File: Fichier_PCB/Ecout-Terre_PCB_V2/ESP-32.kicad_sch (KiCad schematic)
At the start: 43 parts, among them J10 Micro_SD_Card, J13 Conn_GPS, J5 Conn_Alim, J7 Conn_ESP, J8 Conn_ESP, U4 PCM1804, U7 74LVT04, Y1 7V-22.5792MAHV-T

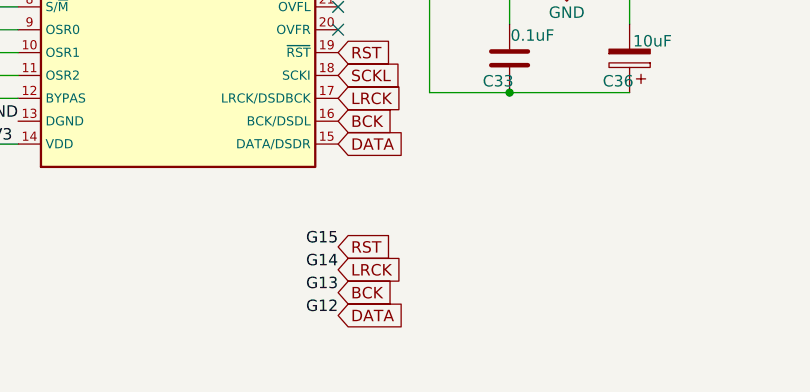
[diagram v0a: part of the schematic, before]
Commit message: Trace pcb
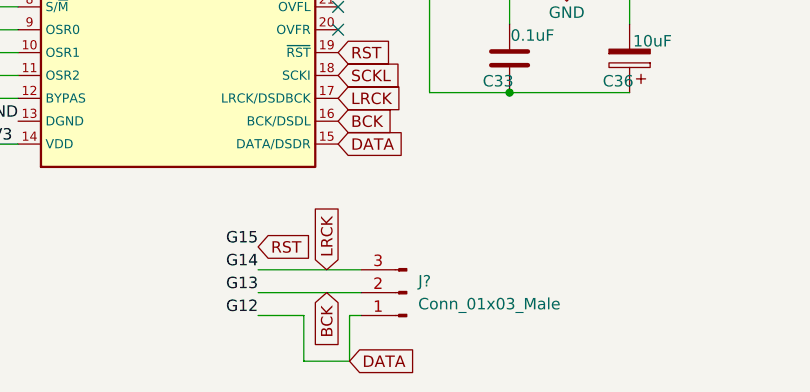
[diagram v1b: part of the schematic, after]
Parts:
- added J?: Conn_01x03_Male, Connector_PinHeader_2.54mm:PinHeader_1x03_P2.54mm_Vertical, symbol Connector:Conn_01x03_Male
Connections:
- net BCK: now also J?.2 (Pin_2)
- net DATA: now also J?.1 (Pin_1)
- net LRCK: now also J?.3 (Pin_3)
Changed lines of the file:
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@@
+    (stroke (width 0) (type default) (color 0 0 0 0))
+  )
+  (wire (pts (xy 97.79 172.72) (xy 102.87 172.72))
     (stroke (width 0) (type default) (color 0 0 0 0))
   )
@@
     (stroke (width 0) (type default) (color 0 0 0 0))
   )
+  (wire (pts (xy 102.87 172.72) (xy 102.87 167.64))
+    (stroke (width 0) (type default) (color 0 0 0 0))
+  )
   (wire (pts (xy 45.085 128.27) (xy 49.53 128.27))
     (stroke (width 0) (type default) (color 0 0 0 0))
@@
     (stroke (width 0) (type default) (color 0 0 0 0))
   )
+  (wire (pts (xy 102.87 167.64) (xy 104.14 167.64))
+    (stroke (width 0) (type default) (color 0 0 0 0))
+  )
   (wire (pts (xy 133.985 128.27) (xy 133.985 135.255))
     (stroke (width 0) (type default) (color 0 0 0 0))
@@
     (stroke (width 0) (type default) (color 0 0 0 0))
   )
+  (wire (pts (xy 92.71 167.64) (xy 97.79 167.64))
+    (stroke (width 0) (type default) (color 0 0 0 0))
+  )
   (wire (pts (xy 111.76 142.875) (xy 120.65 142.875))
     (stroke (width 0) (type default) (color 0 0 0 0))
@@
     (stroke (width 0) (type default) (color 0 0 0 0))
   )
+  (wire (pts (xy 92.71 165.1) (xy 104.14 165.1))
+    (stroke (width 0) (type default) (color 0 0 0 0))
+  )
   (wire (pts (xy 58.42 93.98) (xy 58.42 90.17))
     (stroke (width 0) (type default) (color 0 0 0 0))
@@
     (stroke (width 0) (type default) (color 0 0 0 0))
   )
+  (wire (pts (xy 97.79 167.64) (xy 97.79 172.72))
+    (stroke (width 0) (type default) (color 0 0 0 0))
+  )
   (wire (pts (xy 40.64 62.23) (xy 36.83 62.23))
     (stroke (width 0) (type default) (color 0 0 0 0))
@@
     (stroke (width 0) (type default) (color 0 0 0 0))
   )
+  (wire (pts (xy 92.71 162.56) (xy 104.14 162.56))
+    (stroke (width 0) (type default) (color 0 0 0 0))
+  )
   (wire (pts (xy 173.99 121.92) (xy 182.88 121.92))
     (stroke (width 0) (type default) (color 0 0 0 0))
@@
     (effects (font (size 1.27 1.27)) (justify right bottom))
   )
-  (label "G15" (at 101.6 160.02 180)
+  (label "G15" (at 92.71 160.02 180)
     (effects (font (size 1.27 1.27)) (justify right bottom))
   )
@@
     (effects (font (size 1.27 1.27)) (justify right bottom))
   )
-  (label "G12" (at 101.6 167.64 180)
+  (label "G12" (at 92.71 167.64 180)
     (effects (font (size 1.27 1.27)) (justify right bottom))
   )
@@
     (effects (font (size 1.27 1.27)) (justify left bottom))
   )
-  (label "G14" (at 101.6 162.56 180)
+  (label "G14" (at 92.71 162.56 180)
     (effects (font (size 1.27 1.27)) (justify right bottom))
   )
@@
     (effects (font (size 1.27 1.27)) (justify right bottom))
   )
-  (label "G13" (at 101.6 165.1 180)
+  (label "G13" (at 92.71 165.1 180)
     (effects (font (size 1.27 1.27)) (justify right bottom))
   )
@@
     (effects (font (size 1.27 1.27)) (justify right bottom))
   )
-  (global_label "DATA" (shape input) (at 101.6 167.64 0) (fields_autoplaced)
-    (effects (font (size 1.27 1.27)) (justify left))
-    (property "Intersheet References" "${INTERSHEET_REFS}" (id 0) (at 108.4279 167.5606 0)
+  (global_label "DATA" (shape input) (at 102.87 172.72 0) (fields_autoplaced)
+    (effects (font (size 1.27 1.27)) (justify left))
+    (property "Intersheet References" "${INTERSHEET_REFS}" (id 0) (at 109.6979 172.6406 0)
       (effects (font (size 1.27 1.27)) (justify left) hide)
     )
@@
     )
   )
-  (global_label "LRCK" (shape input) (at 101.6 162.56 0) (fields_autoplaced)
-    (effects (font (size 1.27 1.27)) (justify left))
-    (property "Intersheet References" "${INTERSHEET_REFS}" (id 0) (at 108.8512 162.4806 0)
+  (global_label "LRCK" (shape input) (at 100.33 162.56 90) (fields_autoplaced)
+    (effects (font (size 1.27 1.27)) (justify left))
+    (property "Intersheet References" "${INTERSHEET_REFS}" (id 0) (at 100.2506 155.3088 90)
       (effects (font (size 1.27 1.27)) (justify left) hide)
     )
@@
     )
   )
-  (global_label "BCK" (shape input) (at 101.6 165.1 0) (fields_autoplaced)
-    (effects (font (size 1.27 1.27)) (justify left))
-    (property "Intersheet References" "${INTERSHEET_REFS}" (id 0) (at 107.8231 165.0206 0)
-      (effects (font (size 1.27 1.27)) (justify left) hide)
-    )
-  )
-  (global_label "RST" (shape input) (at 101.6 160.02 0) (fields_autoplaced)
-    (effects (font (size 1.27 1.27)) (justify left))
-    (property "Intersheet References" "${INTERSHEET_REFS}" (id 0) (at 107.4602 159.9406 0)
+  (global_label "BCK" (shape input) (at 100.33 165.1 270) (fields_autoplaced)
+    (effects (font (size 1.27 1.27)) (justify right))
+    (property "Intersheet References" "${INTERSHEET_REFS}" (id 0) (at 100.4094 171.3231 90)
+      (effects (font (size 1.27 1.27)) (justify right) hide)
+    )
+  )
+  (global_label "RST" (shape input) (at 92.71 160.02 0) (fields_autoplaced)
+    (effects (font (size 1.27 1.27)) (justify left))
+    (property "Intersheet References" "${INTERSHEET_REFS}" (id 0) (at 98.5702 159.9406 0)
       (effects (font (size 1.27 1.27)) (justify left) hide)
     )
@@
     (pin "2")
   )
+  (symbol (lib_id "Connector:Conn_01x03_Male") (at 109.22 165.1 180) (unit 1)
+    (in_bom yes) (on_board yes) (fields_autoplaced)
+    (property "Reference" "J?" (id 0) (at 110.49 163.8299 0)
+      (effects (font (size 1.27 1.27)) (justify right))
+    )
+    (property "Value" "Conn_01x03_Male" (id 1) (at 110.49 166.3699 0)
+      (effects (font (size 1.27 1.27)) (justify right))
+    )
+    (property "Footprint" "Connector_PinHeader_2.54mm:PinHeader_1x03_P2.54mm_Vertical" (id 2) (at 109.22 165.1 0)
+      (effects (font (size 1.27 1.27)) hide)
+    )
+    (property "Datasheet" "~" (id 3) (at 109.22 165.1 0)
+      (effects (font (size 1.27 1.27)) hide)
+    )
+    (pin "1")
+    (pin "2")
+    (pin "3")
+  )
   (symbol (lib_id "Device:C_Polarized") (at 133.985 139.065 180) (unit 1)

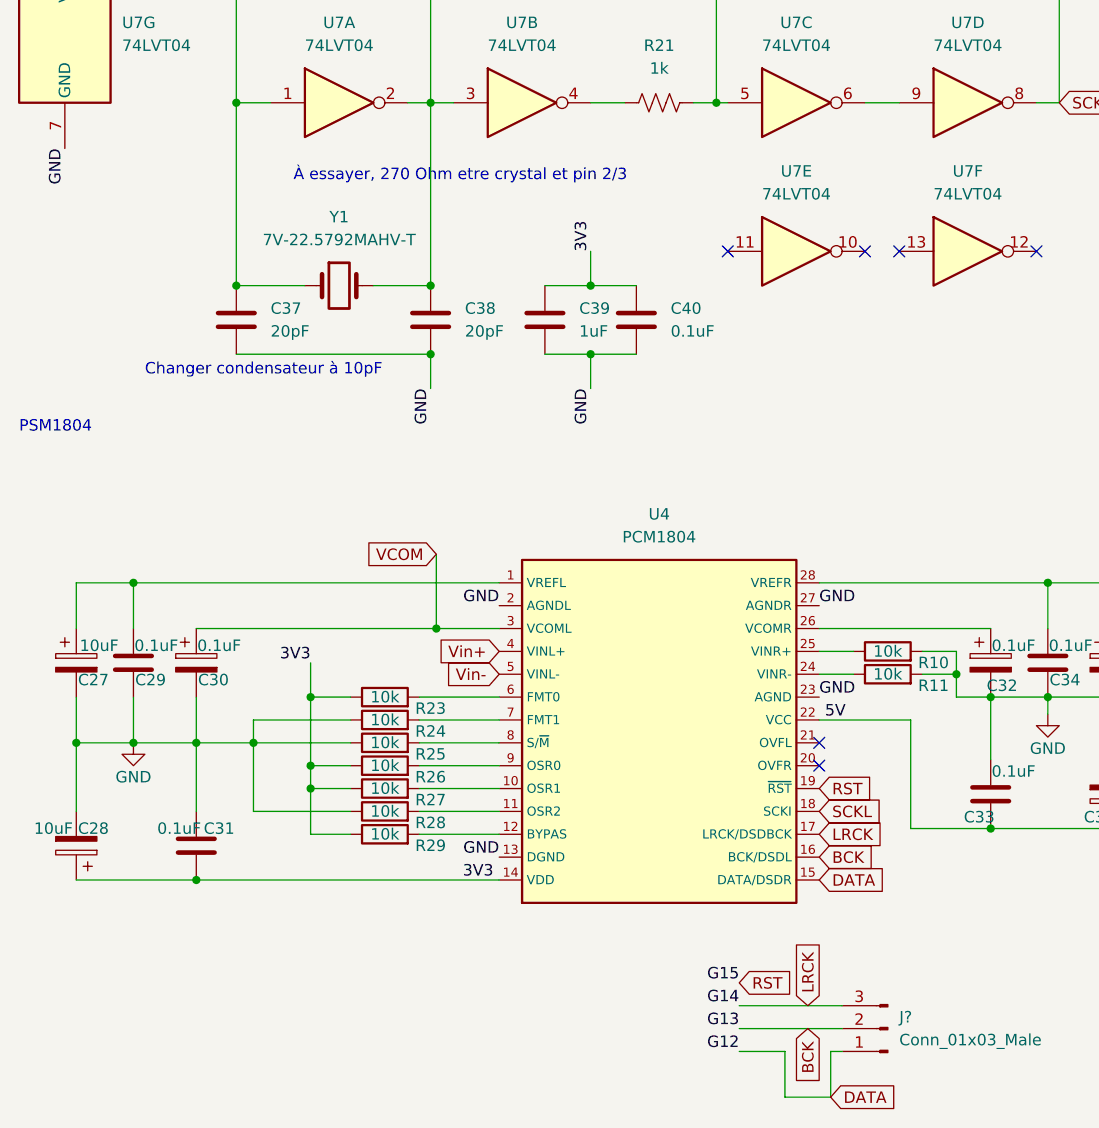
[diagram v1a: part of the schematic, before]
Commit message: Envoie de code et correction PCB
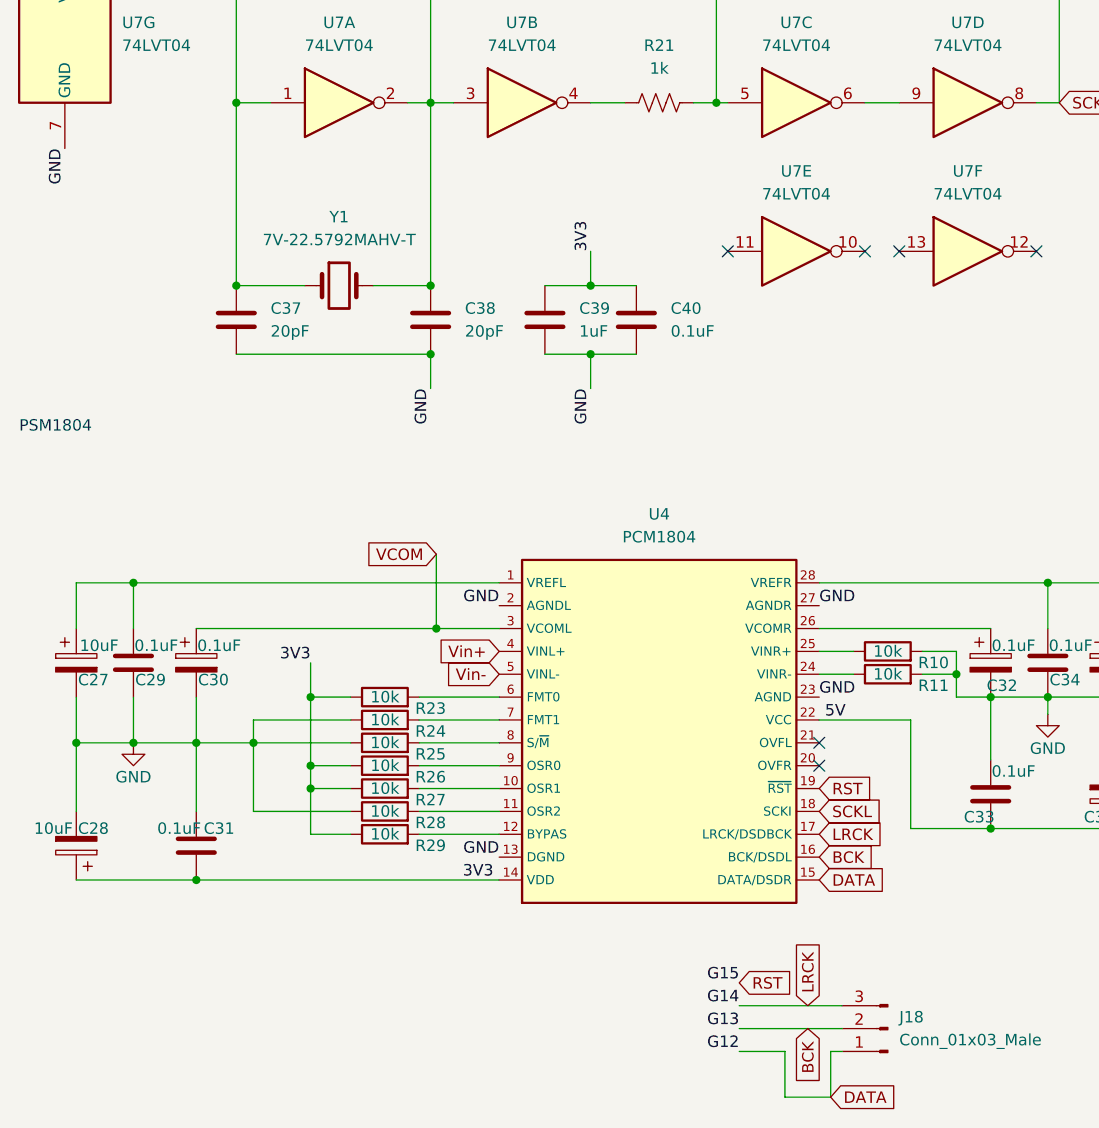
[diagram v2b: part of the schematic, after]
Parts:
- gave numbers to parts that had none: 1
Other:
- note removed: "Changer condensateur à 10pF"
- note removed: "À essayer, 270 Ohm etre crystal et pin 2/3"
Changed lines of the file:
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@@
-    (effects (font (size 1.27 1.27)) (justify left bottom))
-  )
-  (text "Changer condensateur à 10pF" (at 26.67 92.71 0)
     (effects (font (size 1.27 1.27)) (justify left bottom))
   )
@@
   )
   (text "PSM1804" (at 12.7 99.06 0)
-    (effects (font (size 1.27 1.27)) (justify left bottom))
-  )
-  (text "À essayer, 270 Ohm etre crystal et pin 2/3" (at 43.18 71.12 0)
     (effects (font (size 1.27 1.27)) (justify left bottom))
   )
@@
   (symbol (lib_id "Connector:Conn_01x03_Male") (at 109.22 165.1 180) (unit 1)
     (in_bom yes) (on_board yes) (fields_autoplaced)
-    (property "Reference" "J?" (id 0) (at 110.49 163.8299 0)
+    (property "Reference" "J18" (id 0) (at 110.49 163.8299 0)
       (effects (font (size 1.27 1.27)) (justify right))
     )
